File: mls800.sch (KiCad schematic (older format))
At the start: 50 parts, among them CON1 BARREL_JACK, IC1 6N137, J1 USB, P1 CONN_02X03, P2 DIN_5, P3 DIN_5, SW1 SW_PUSH, SW2 SW_TACT_LED, SW3 SW_TACT_LED, U1 LM340-5.0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

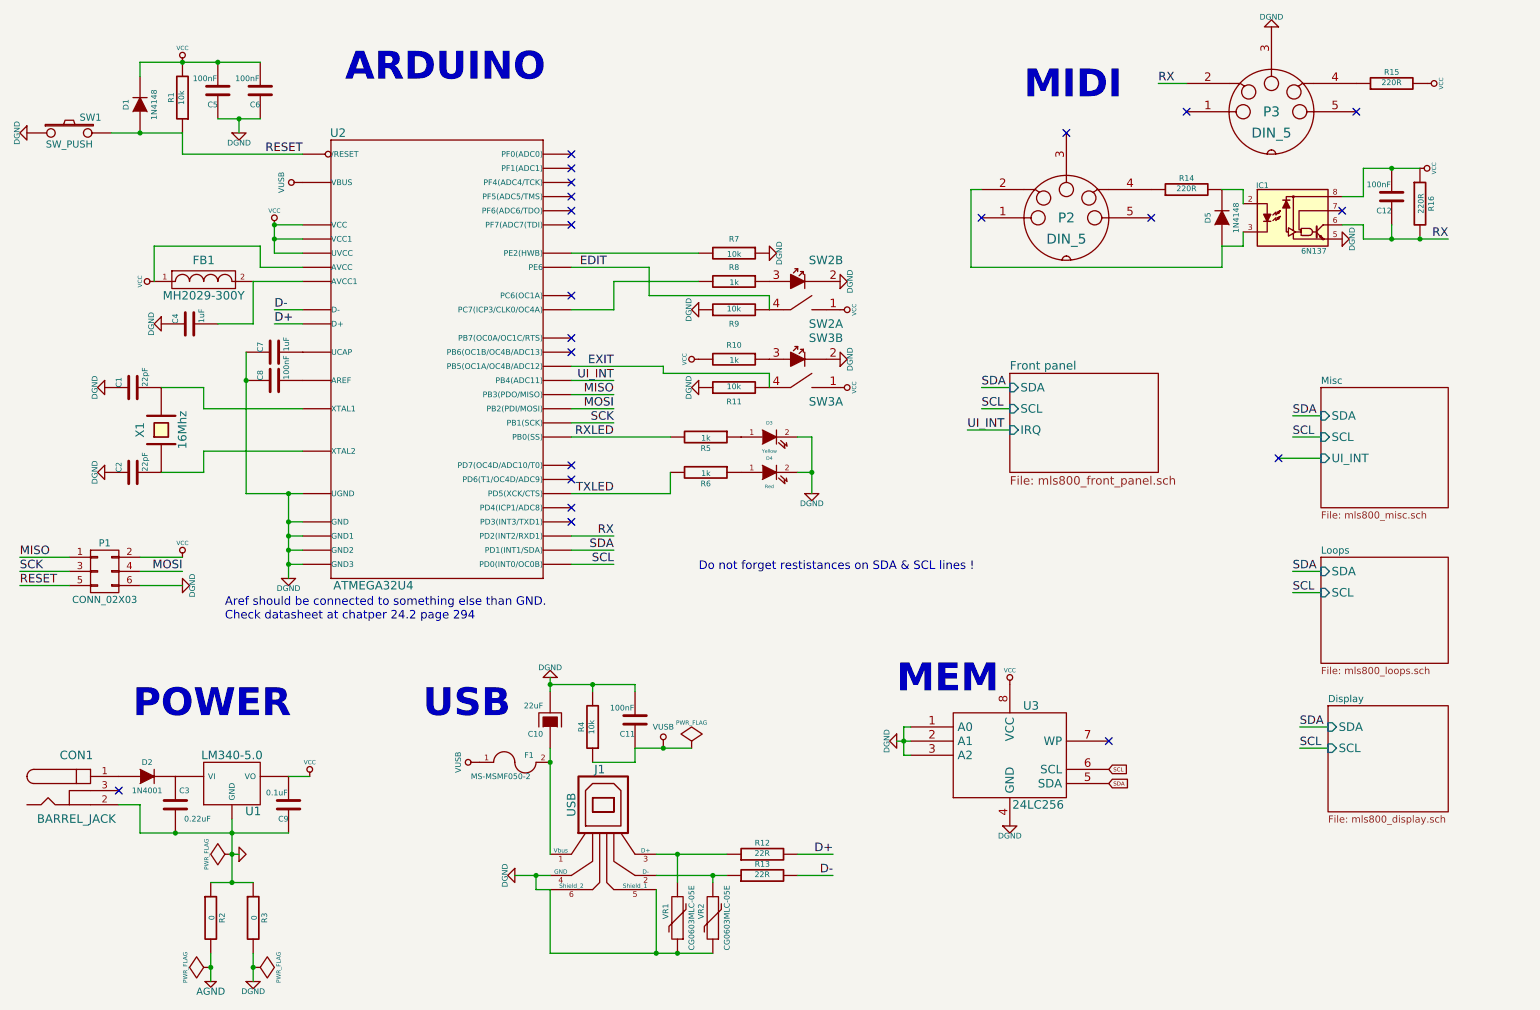
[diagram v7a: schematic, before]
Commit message: MLS800
* updated layout to match AS1115 diagrams
* added pull-up resistors
* removed useless sheets
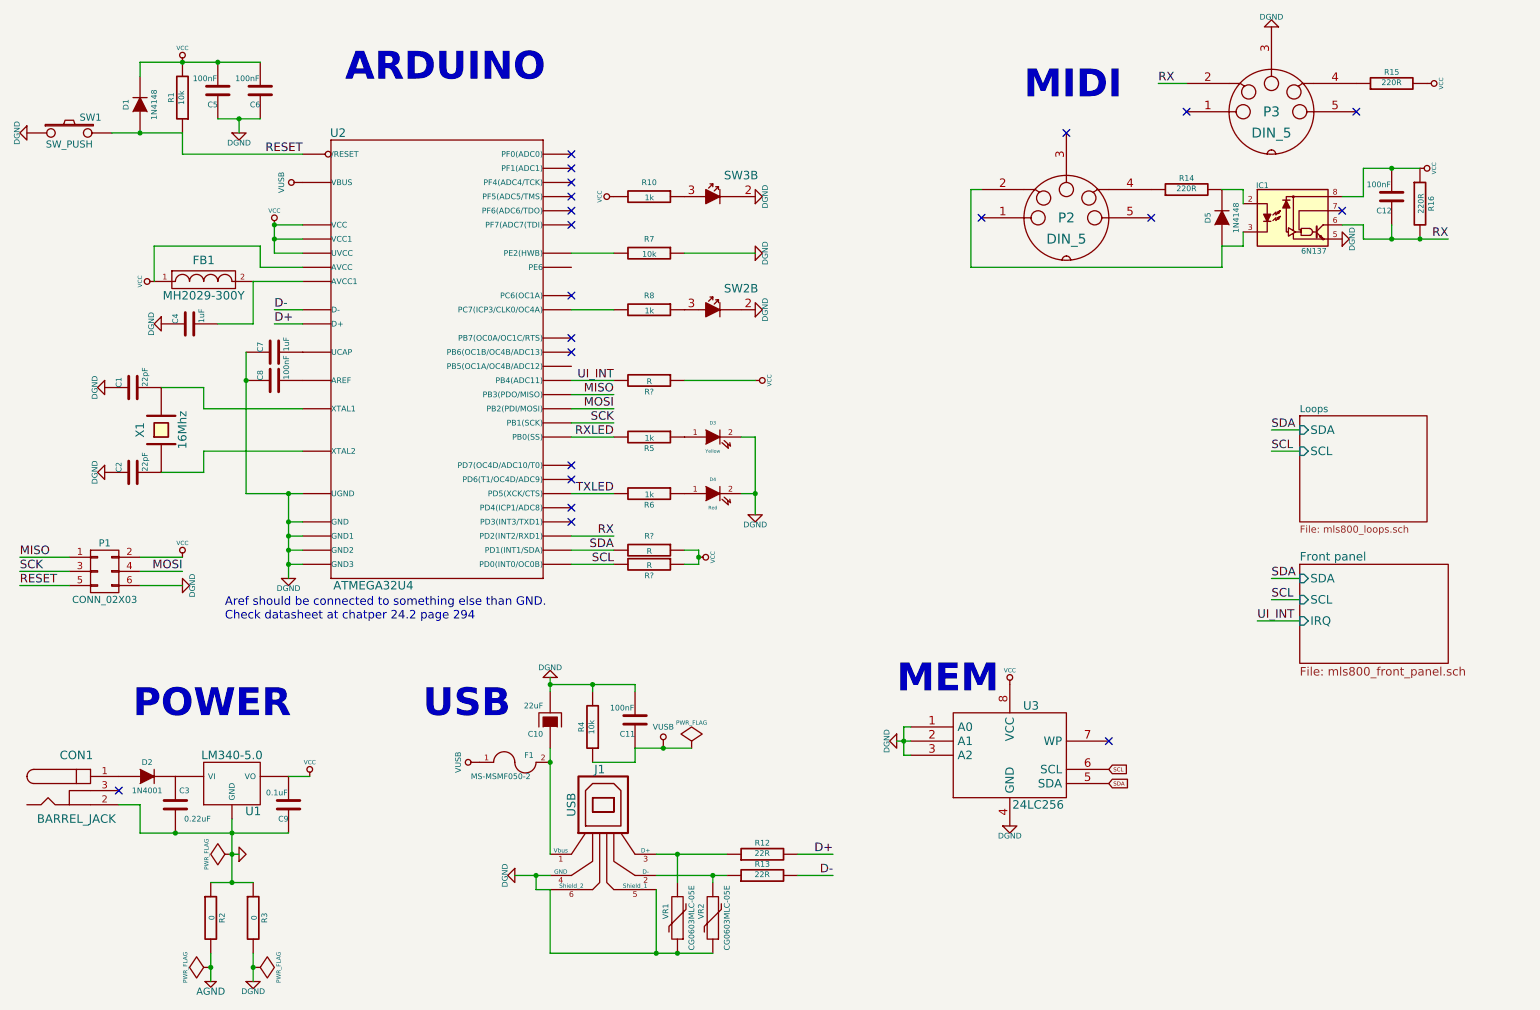
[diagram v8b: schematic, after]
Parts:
- removed R11, R9: 10k, Resistors_SMD:R_0805_HandSoldering, symbol R
- removed unit 1 of SW2
- removed unit 1 of SW3
- added R? (x3): R, symbol R
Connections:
- net SCL: now also R?.2
- net SDA: now also R?.2
- net UI_INT: now also R?.2
- net VCC: now also R?.1, R?.1, R?.1
- net EDIT: no longer names the net of U2.1 (PE6)
- net EXIT: no longer names the net of U2.29 (PB5(OC1A/OC4B/ADC12))
- no-connect marks 22 -> 21
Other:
- note removed: "Do not forget restistances on SDA & SCL lines !"
- moved on the sheet: D3, D4, R10, R5, R6, R7, R8, SW2B, SW3B
